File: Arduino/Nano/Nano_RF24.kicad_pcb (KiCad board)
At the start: 2 copper layers, 35.1 x 40 mm, 6 parts, among them P1 NRF24L01+, U1 Arduino Nano

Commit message: Update URLs and images
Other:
- board text added: "github.com/markjb/NRF24L01_Adaptors"
- board text removed: "github.com/markjb/url?"
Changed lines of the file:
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@@
     (comment 1 "Copyright Mark Benson 2016")
     (comment 2 "License Creative Commons Attribution Non Commerical 4.0 (CCNCBY 4.0)")
-    (comment 3 github.com/markjb/url)
+    (comment 3 github.com/markjb/NRF24L01_Adaptors)
   )
   (layers
@@
       (effects (font (size 1 1) (thickness 0.15)))
     )
-    (fp_text value 100uF (at 1.25 3.8 180) (layer F.SilkS)
+    (fp_text value 100uF (at 3.7592 3.4036 180) (layer F.SilkS)
       (effects (font (size 1 1) (thickness 0.15)))
     )
@@
     (effects (font (size 1 1) (thickness 0.15)) (justify mirror))
   )
-  (gr_text github.com/markjb/url? (at 136.5504 60.4012 90) (layer B.SilkS)
-    (effects (font (size 1 1) (thickness 0.15)) (justify mirror))
-  )
-  (gr_text github.com/markjb/url? (at 136.7536 60.2996 90) (layer F.SilkS)
-    (effects (font (size 1 1) (thickness 0.15)))
+  (gr_text github.com/markjb/NRF24L01_Adaptors (at 136.652 61.722 90) (layer B.SilkS)
+    (effects (font (size 0.8 0.8) (thickness 0.15)) (justify mirror))
+  )
+  (gr_text github.com/markjb/NRF24L01_Adaptors (at 136.652 61.722 90) (layer F.SilkS)
+    (effects (font (size 0.8 0.8) (thickness 0.15)))
   )
   (gr_text "Arduino Nano NRF24L01 adaptor" (at 134.874 61.722 90) (layer F.SilkS)

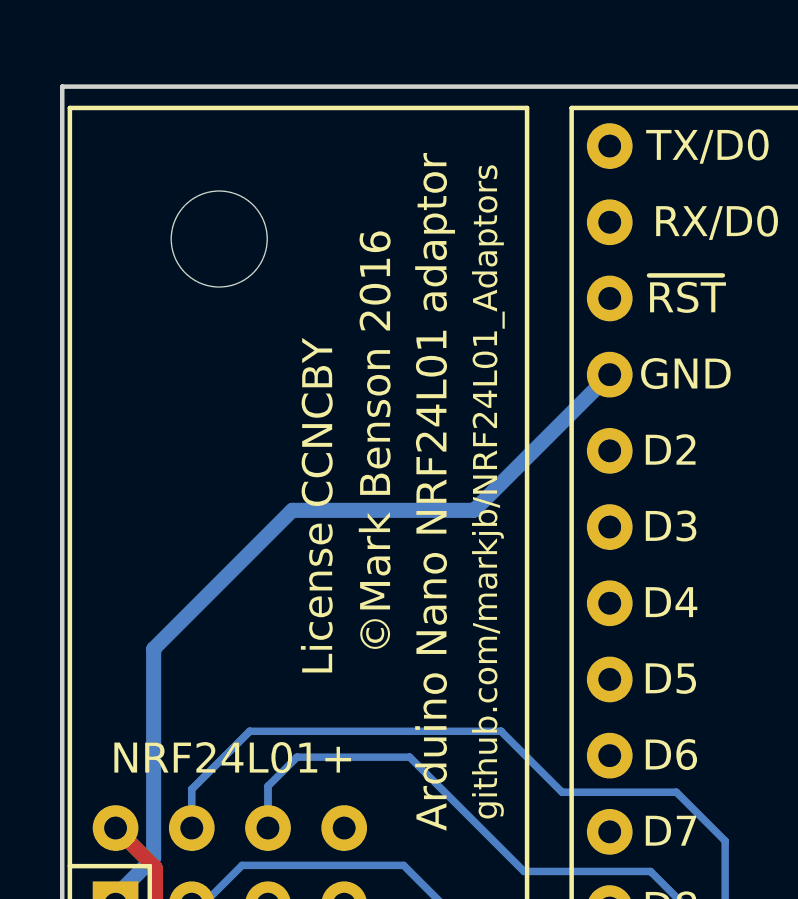
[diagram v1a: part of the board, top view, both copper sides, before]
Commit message: Updated licence and copyright
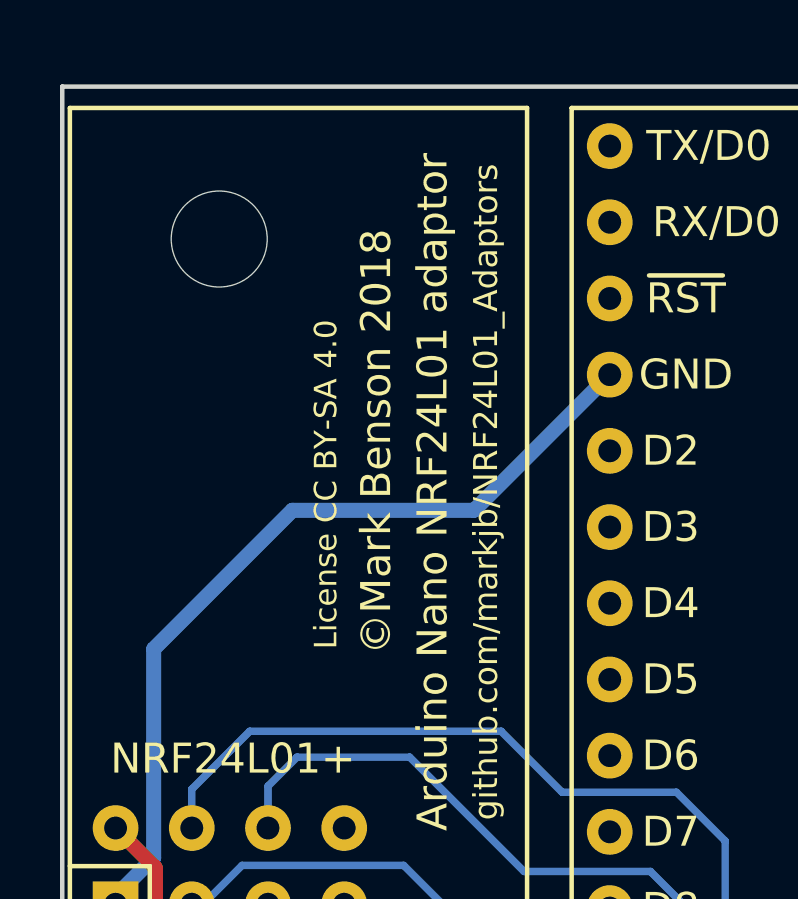
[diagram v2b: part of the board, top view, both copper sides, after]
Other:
- board text added: "License CC BY-SA 4.0"
- board text added: "©Mark Benson 2018"
- board text removed: "License CCNCBY"
- board text removed: "©Mark Benson 2016"
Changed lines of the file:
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@@
-(kicad_pcb (version 4) (host pcbnew 4.0.2-stable)
+(kicad_pcb (version 4) (host pcbnew 4.0.7-e2-6376~58~ubuntu16.04.1)
   (general
     (links 9)
     (no_connects 0)
-    (area 122.454599 48.134199 157.707401 88.263801)
+    (area 118.204857 48.1142 158.451943 88.6886)
     (thickness 1.6)
     (drawings 12)
@@
   (title_block
     (title "Arduino Nano NRF24L01+ Adaptor")
-    (date 2016-08-15)
+    (date 2018-03-30)
     (rev 1)
-    (comment 1 "Copyright Mark Benson 2016")
-    (comment 2 "License Creative Commons Attribution Non Commerical 4.0 (CCNCBY 4.0)")
+    (comment 1 "Copyright Mark Benson 2018")
+    (comment 2 "License Creative Commons Attribution ShareAlike 4.0 (CC BY-SA 4.0)")
     (comment 3 github.com/markjb/NRF24L01_Adaptors)
   )
   (layers
-    (0 F.Cu signal)
-    (31 B.Cu signal)
-    (32 B.Adhes user)
-    (33 F.Adhes user)
-    (34 B.Paste user)
-    (35 F.Paste user)
+    (0 F.Cu signal hide)
+    (31 B.Cu signal hide)
+    (32 B.Adhes user hide)
+    (33 F.Adhes user hide)
+    (34 B.Paste user hide)
+    (35 F.Paste user hide)
     (36 B.SilkS user)
-    (37 F.SilkS user)
+    (37 F.SilkS user hide)
     (38 B.Mask user)
     (39 F.Mask user)
@@
     (visible_elements 7FFFFFFF)
     (pcbplotparams
-      (layerselection 0x00030_80000001)
-      (usegerberextensions false)
+      (layerselection 0x010f0_80000001)
+      (usegerberextensions true)
       (excludeedgelayer true)
       (linewidth 0.100000)
@@
       (outputformat 1)
       (mirror false)
-      (drillshape 1)
+      (drillshape 0)
       (scaleselection 1)
-      (outputdirectory ""))
+      (outputdirectory gerber/))
   )
   (net 0 "")
@@
     (pad 1 np_thru_hole circle (at 0 0) (size 3.2 3.2) (drill 3.2) (layers *.Cu *.Mask F.SilkS))
   )
-  (gr_text "License CCNCBY" (at 131.064 62.23 90) (layer B.SilkS)
-    (effects (font (size 1 1) (thickness 0.15)) (justify mirror))
-  )
-  (gr_text "License CCNCBY" (at 131.064 62.23 90) (layer F.SilkS)
-    (effects (font (size 1 1) (thickness 0.15)))
-  )
-  (gr_text "©Mark Benson 2016" (at 132.8928 60.5028 90) (layer B.SilkS)
+  (gr_text "License CC BY-SA 4.0" (at 131.064 61.976 90) (layer B.SilkS)
+    (effects (font (size 0.75 0.75) (thickness 0.15)) (justify mirror))
+  )
+  (gr_text "License CC BY-SA 4.0" (at 131.318 61.468 90) (layer F.SilkS)
+    (effects (font (size 0.75 0.75) (thickness 0.15)))
+  )
+  (gr_text "©Mark Benson 2018" (at 132.8928 60.5028 90) (layer B.SilkS)
     (effects (font (size 1 1) (thickness 0.15)) (justify mirror))
   )
@@
     (effects (font (size 1 1) (thickness 0.15)))
   )
-  (gr_text "©Mark Benson 2016" (at 132.9944 60.0456 90) (layer F.SilkS)
+  (gr_text "©Mark Benson 2018" (at 132.9944 60.0456 90) (layer F.SilkS)
     (effects (font (size 1 1) (thickness 0.15)))
   )

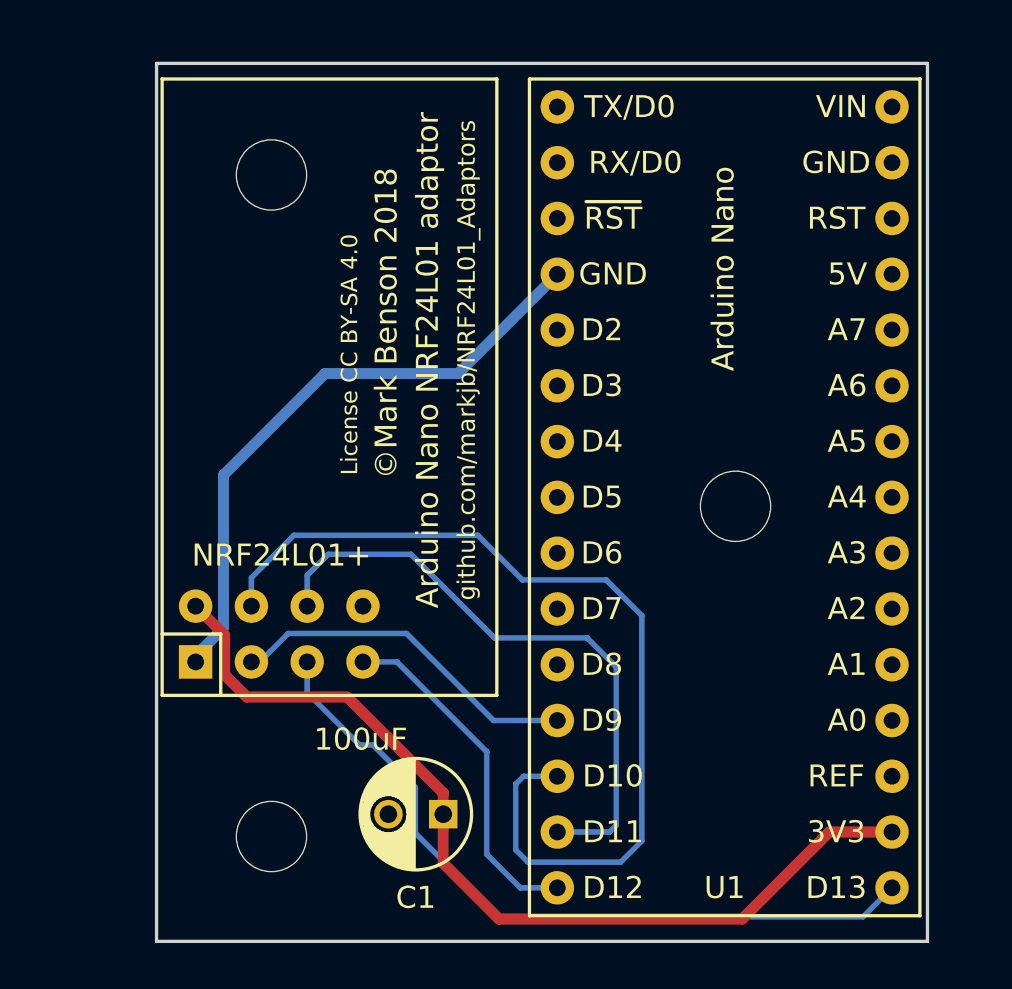
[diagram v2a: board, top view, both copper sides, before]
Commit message: v2 with breakout pins
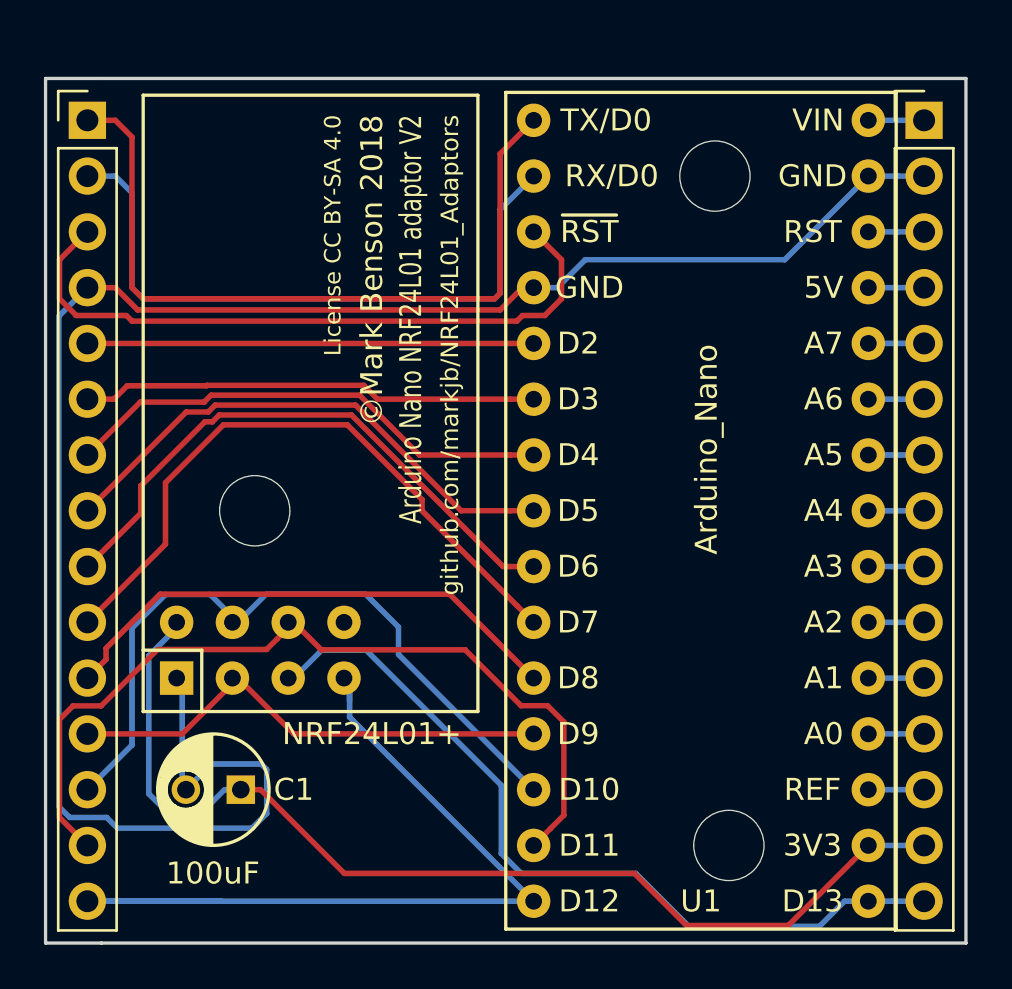
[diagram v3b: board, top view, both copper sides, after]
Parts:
- added J1: Conn_01x15, Pin_Headers:Pin_Header_Straight_1x15_Pitch2.54mm, F.Cu at (119.4, 50.8)
- added J2: Conn_01x15, Pin_Headers:Pin_Header_Straight_1x15_Pitch2.54mm, F.Cu at (157.5, 50.8)
- U1: value Arduino Nano -> Arduino_Nano
- moved REF** 21.9 mm to (127.0, 68.6)
- moved REF** 20.8 mm to (148.6, 83.8)
- moved REF** 20.2 mm to (148.0, 53.3)
- moved C1 9.29 mm to (126.4, 81.3)
- moved U1 1.24 mm to (147.3, 66.0)
- moved P1 1.14 mm to (129.3, 62.9)
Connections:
- U1 pad 29: Net-(U1-Pad29) -> Net-(C1-Pad2)
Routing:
- net Net-(C1-Pad2): track 28.0 -> 86.8 mm
- net Net-(J1-Pad1): track 0.00 -> 34.8 mm
- net Net-(J1-Pad3): track 0.00 -> 30.8 mm
- net Net-(J1-Pad2): track 0.00 -> 29.7 mm
- net Net-(J1-Pad10): track 0.00 -> 29.7 mm
- net Net-(J1-Pad9): track 0.00 -> 26.8 mm
- net Net-(J1-Pad15): track 15.9 -> 41.1 mm
- net Net-(J1-Pad8): track 0.00 -> 24.3 mm
- net Net-(J1-Pad11): track 0.00 -> 23.8 mm
- net Net-(J1-Pad7): track 0.00 -> 22.6 mm
- net Net-(J1-Pad6): track 0.00 -> 20.8 mm
- net Net-(J1-Pad5): track 0.00 -> 20.3 mm
- net Net-(J1-Pad13): track 43.3 -> 32.6 mm
- net Net-(J1-Pad14): track 28.6 -> 39.1 mm
- net Net-(C1-Pad1): track 42.4 -> 48.8 mm
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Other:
- board size 35.1 x 40 mm -> 41.9 x 39.4 mm
- board text added: "Arduino Nano NRF24L01 adaptor V2"
- board text removed: "Arduino Nano NRF24L01 adaptor"
